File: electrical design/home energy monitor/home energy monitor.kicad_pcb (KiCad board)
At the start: 2 copper layers, 50 x 20 mm, 25 parts, among them J4 Conn_01x07_Socket, J5 Conn_01x07_Socket

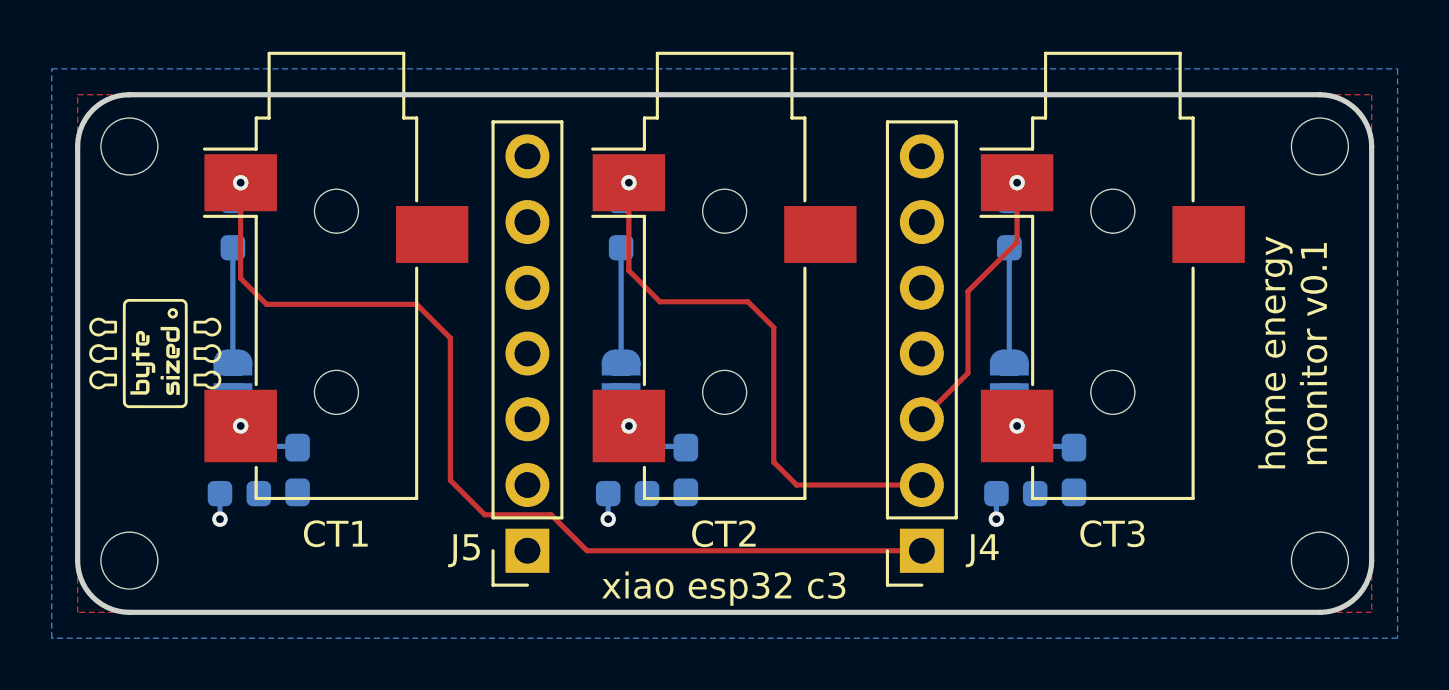
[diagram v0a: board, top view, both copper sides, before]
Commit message: Added PCB routing for alternate ADC pins
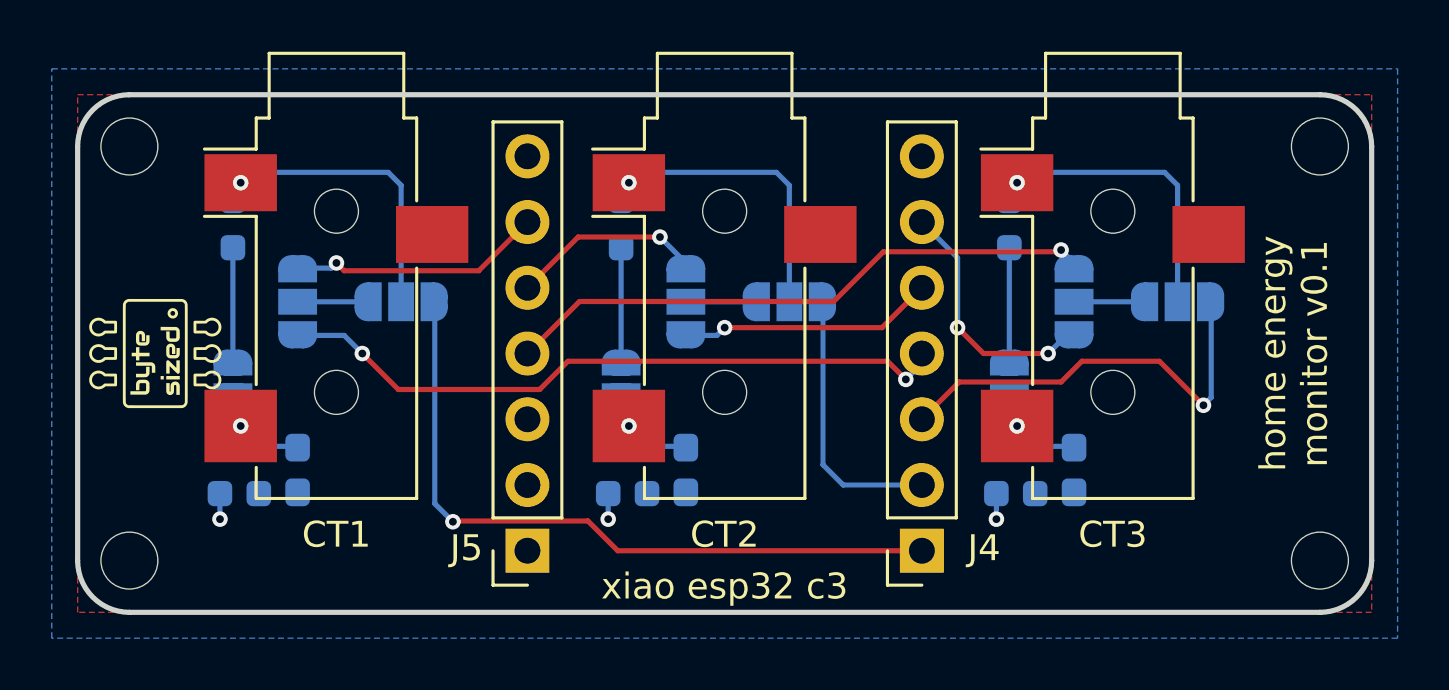
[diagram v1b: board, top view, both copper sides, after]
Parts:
- added JP4: SolderJumper_3_Open, Jumper:SolderJumper-3_P1.3mm_Open_RoundedPad1.0x1.5mm_NumberLabels, B.Cu at (137.5, 98.0)
- added JP5: SolderJumper_3_Open, Jumper:SolderJumper-3_P1.3mm_Open_RoundedPad1.0x1.5mm_NumberLabels, B.Cu at (133.5, 98.0)
- added JP6: SolderJumper_3_Open, Jumper:SolderJumper-3_P1.3mm_Open_RoundedPad1.0x1.5mm_NumberLabels, B.Cu at (152.5, 98.0)
- added JP7: SolderJumper_3_Open, Jumper:SolderJumper-3_P1.3mm_Open_RoundedPad1.0x1.5mm_NumberLabels, B.Cu at (148.5, 98.0)
- added JP8: SolderJumper_3_Open, Jumper:SolderJumper-3_P1.3mm_Open_RoundedPad1.0x1.5mm_NumberLabels, B.Cu at (167.5, 98.0)
- added JP9: SolderJumper_3_Open, Jumper:SolderJumper-3_P1.3mm_Open_RoundedPad1.0x1.5mm_NumberLabels, B.Cu at (163.5, 98.0)
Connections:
- net VCC renamed 3.3V
- CT1 pad S: /ADC1 -> Net-(JP4-C)
- CT2 pad S: /ADC2 -> Net-(JP6-C)
- CT3 pad S: /ADC3 -> Net-(JP8-C)
- J4 pad 4: unconnected-(J4-Pin_4-Pad4) -> /ADC4
- J4 pad 5: unconnected-(J4-Pin_5-Pad5) -> /ADC5
- J4 pad 6: unconnected-(J4-Pin_6-Pad6) -> /ADC6
- J5 pad 4: unconnected-(J5-Pin_4-Pad4) -> /ADC9
- J5 pad 5: unconnected-(J5-Pin_5-Pad5) -> /ADC8
- J5 pad 6: unconnected-(J5-Pin_6-Pad6) -> /ADC7
- R1 pad 1: /ADC1 -> Net-(JP4-C)
- R2 pad 1: /ADC2 -> Net-(JP6-C)
- R3 pad 1: /ADC3 -> Net-(JP8-C)
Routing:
- net /ADC4: track 0.00 -> 26.4 mm, vias 0 -> 2
- net /ADC9: track 0.00 -> 23.2 mm, vias 0 -> 1
- net Net-(JP4-C): track 0.00 -> 11.9 mm, vias 0 -> 1
- net Net-(JP8-C): track 0.00 -> 11.9 mm, vias 0 -> 1
- net Net-(JP6-C): track 0.00 -> 11.9 mm, vias 0 -> 1
- net /ADC2: track 22.0 -> 10.4 mm, vias 1 -> 0
- net /ADC1: track 38.4 -> 27.4 mm
- net /ADC5: track 0.00 -> 9.88 mm, vias 0 -> 1
- net /ADC7: track 0.00 -> 9.87 mm, vias 0 -> 1
- net /ADC6: track 0.00 -> 9.86 mm, vias 0 -> 2
- net /ADC8: track 0.00 -> 7.55 mm, vias 0 -> 1
- net /ADC3: track 11.5 -> 16.6 mm
- net Net-(JP8-B): track 0.00 -> 2.70 mm
- net Net-(JP6-B): track 0.00 -> 2.70 mm
- net Net-(JP4-B): track 0.00 -> 2.70 mm
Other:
- board text removed: "If connected current transformers do NOT have internal burden resistors, bridge jumper pads and populate R1, R2, R3"
